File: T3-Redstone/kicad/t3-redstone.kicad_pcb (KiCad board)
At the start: 4 copper layers, 65 x 56.5 mm, 5 parts, among them J1 GEMSTONE_40PIN

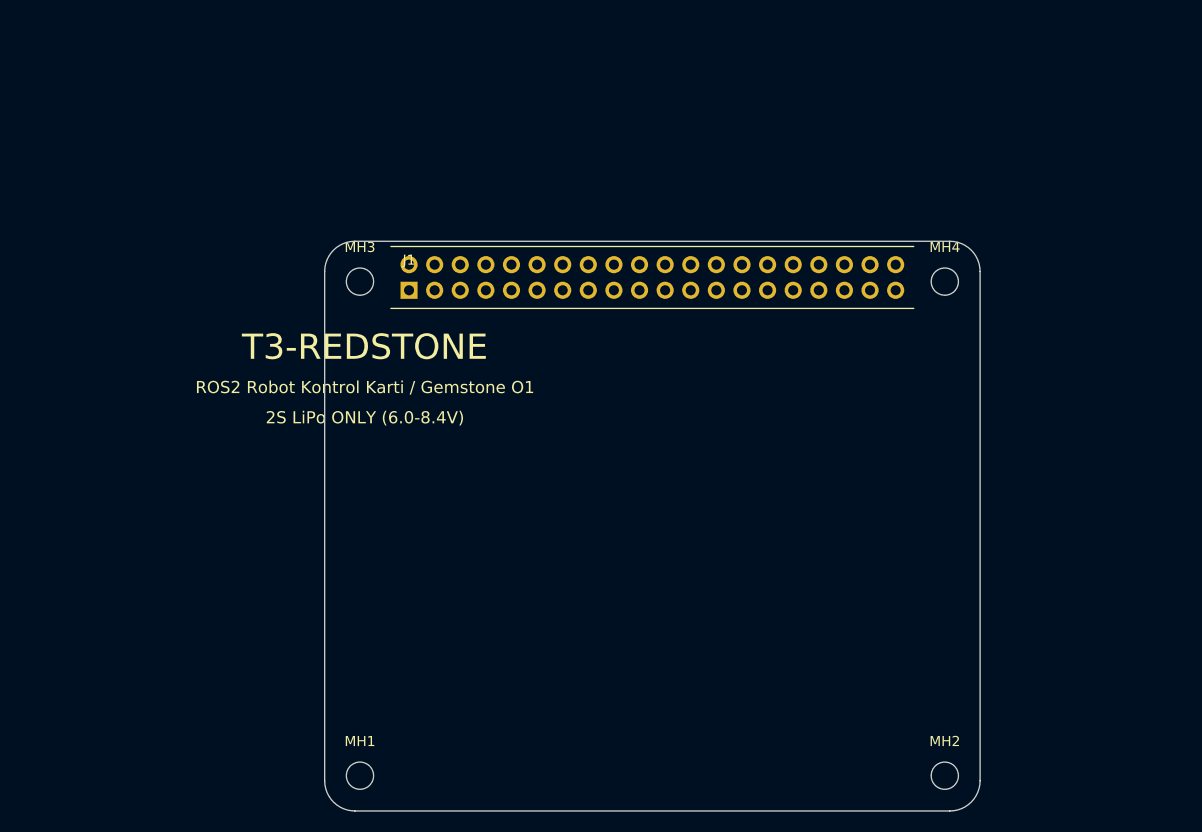
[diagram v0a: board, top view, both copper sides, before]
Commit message: Redstone: tam boy 85x56, kamera/DSI kesiti, 2x20 disi soket
- Kart 65x56.5 (RPi HAT) yerine Gemstone ile ayni tam boy 85x56 mm
- Alt kenara acik U kesit: J4 (CSI) ve J12 (CSI/DSI) konnektorlerine
  kablo ve parmak erisimi. Konum parametrik (CUT_X1/CUT_X2/CUT_DEPTH),
  fotograftan tahmin - kumpasla dogrulanacak
- 2x20 erkek header yerine disi soket (PinSocket_2x20)
- Tam boy shield USB-A yigini ve RJ45 uzerinden gectigi icin en az 16mm
  gecis yuksekliginde soket ve standoff sart; Dwgs.User katmaninda
  yuksek konnektor bolgeleri isaretlendi
- Edge.Cuts konturu kapali dogrulandi (14 segment, 85.00x56.00)

Co-Authored-By: Claude Opus 5 <noreply@anthropic.com>
Claude-Session: https://claude.ai/code/session_01BKimLRXBxXq2q9hJZXs5Qz
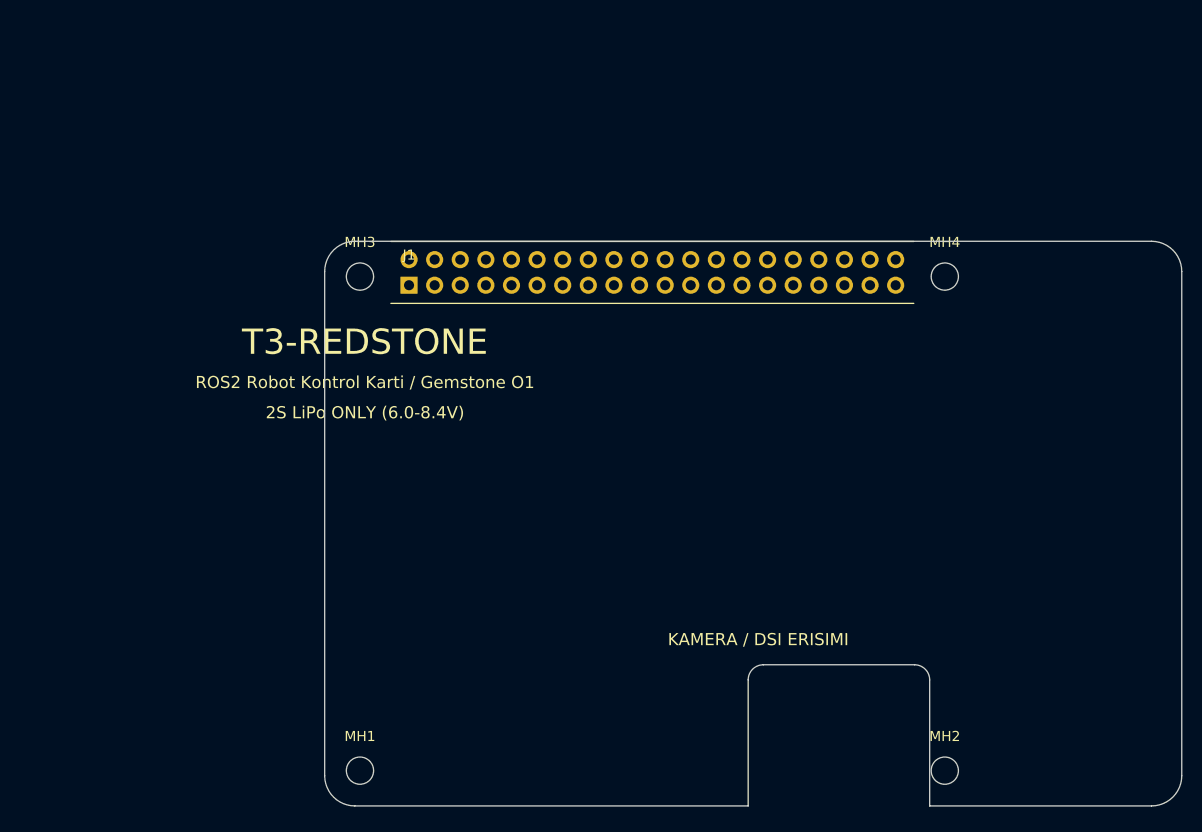
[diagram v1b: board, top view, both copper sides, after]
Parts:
- J1: value GEMSTONE_40PIN -> GEMSTONE_40PIN_DISI_YUKSEK; footprint Connector_PinHeader_2.54mm:PinHeader_2x20_P2.54mm_Vertical -> Connector_PinSocket_2.54mm:PinSocket_2x20_P2.54mm_Vertical
- moved J1 0.50 mm to (58.4, 54.4)
- moved MH1 0.50 mm to (53.5, 102.5)
- moved MH2 0.50 mm to (111.5, 102.5)
- moved MH3 0.50 mm to (53.5, 53.5)
- moved MH4 0.50 mm to (111.5, 53.5)
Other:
- board size 65 x 56.5 mm -> 85 x 56 mm
- board text added: "KAMERA / DSI ERISIMI"
- board text added: "RJ45 Gigabit - h~13.5mm - YUKSEK HEADER SART"
- board text added: "SHIELD = GEMSTONE O1 TAM BOY 85x56"
- board text added: "USB-A x3 yigini - h~13.5mm - YUKSEK HEADER SART"
- board text removed: "GEMSTONE O1 KONTURU 85x56 (referans)"
- board text removed: "USB-A + RJ45 BOLGESI - shield buraya UZANMAMALI (h~13.5mm)"
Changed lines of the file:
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@@
       (subtractmaskfromsilk no) (outputformat 1) (mirror no) (drillshape 1) (scaleselection 1) (outputdirectory "")))
   (net 0 "")
-  (gr_line (start 53.0000 106.5000) (end 112.0000 106.5000) (stroke (width 0.1) (type solid)) (layer "Edge.Cuts"))
-  (gr_line (start 115.0000 103.5000) (end 115.0000 53.0000) (stroke (width 0.1) (type solid)) (layer "Edge.Cuts"))
-  (gr_line (start 112.0000 50.0000) (end 53.0000 50.0000) (stroke (width 0.1) (type solid)) (layer "Edge.Cuts"))
-  (gr_line (start 50.0000 53.0000) (end 50.0000 103.5000) (stroke (width 0.1) (type solid)) (layer "Edge.Cuts"))
-  (gr_arc (start 112.0000 106.5000) (mid 114.1213 105.6213) (end 115.0000 103.5000) (stroke (width 0.1) (type solid)) (layer "Edge.Cuts"))
-  (gr_arc (start 115.0000 53.0000) (mid 114.1213 50.8787) (end 112.0000 50.0000) (stroke (width 0.1) (type solid)) (layer "Edge.Cuts"))
+  (gr_line (start 135.0000 103.0000) (end 135.0000 53.0000) (stroke (width 0.1) (type solid)) (layer "Edge.Cuts"))
+  (gr_line (start 132.0000 50.0000) (end 53.0000 50.0000) (stroke (width 0.1) (type solid)) (layer "Edge.Cuts"))
+  (gr_line (start 50.0000 53.0000) (end 50.0000 103.0000) (stroke (width 0.1) (type solid)) (layer "Edge.Cuts"))
+  (gr_arc (start 132.0000 106.0000) (mid 134.1213 105.1213) (end 135.0000 103.0000) (stroke (width 0.1) (type solid)) (layer "Edge.Cuts"))
+  (gr_arc (start 135.0000 53.0000) (mid 134.1213 50.8787) (end 132.0000 50.0000) (stroke (width 0.1) (type solid)) (layer "Edge.Cuts"))
   (gr_arc (start 53.0000 50.0000) (mid 50.8787 50.8787) (end 50.0000 53.0000) (stroke (width 0.1) (type solid)) (layer "Edge.Cuts"))
-  (gr_arc (start 50.0000 103.5000) (mid 50.8787 105.6213) (end 53.0000 106.5000) (stroke (width 0.1) (type solid)) (layer "Edge.Cuts"))
-  (gr_line (start 50.0000 106.5000) (end 135.0000 106.5000) (stroke (width 0.15) (type solid)) (layer "Dwgs.User"))
-  (gr_line (start 135.0000 106.5000) (end 135.0000 50.5000) (stroke (width 0.15) (type solid)) (layer "Dwgs.User"))
-  (gr_line (start 135.0000 50.5000) (end 50.0000 50.5000) (stroke (width 0.15) (type solid)) (layer "Dwgs.User"))
-  (gr_line (start 50.0000 50.5000) (end 50.0000 106.5000) (stroke (width 0.15) (type solid)) (layer "Dwgs.User"))
-  (gr_text "GEMSTONE O1 KONTURU 85x56 (referans)" (at 84.0000 110.0000) (layer "Dwgs.User") (effects (font (size 1.2 1.2) (thickness 0.25))))
-  (gr_line (start 115.0000 106.5000) (end 135.0000 106.5000) (stroke (width 0.3) (type solid)) (layer "Dwgs.User"))
-  (gr_line (start 135.0000 106.5000) (end 135.0000 50.5000) (stroke (width 0.3) (type solid)) (layer "Dwgs.User"))
-  (gr_line (start 135.0000 50.5000) (end 115.0000 50.5000) (stroke (width 0.3) (type solid)) (layer "Dwgs.User"))
-  (gr_line (start 115.0000 50.5000) (end 115.0000 106.5000) (stroke (width 0.3) (type solid)) (layer "Dwgs.User"))
-  (gr_text "USB-A + RJ45 BOLGESI - shield buraya UZANMAMALI (h~13.5mm)" (at 125.0000 78.5000) (layer "Dwgs.User") (effects (font (size 1.0 1.0) (thickness 0.25))))
-  (footprint "MountingHole:MountingHole_2.7mm_M2.5" (layer "F.Cu") (at 53.5000 103.0000)
+  (gr_arc (start 50.0000 103.0000) (mid 50.8787 105.1213) (end 53.0000 106.0000) (stroke (width 0.1) (type solid)) (layer "Edge.Cuts"))
+  (gr_line (start 53.0000 106.0000) (end 92.0000 106.0000) (stroke (width 0.1) (type solid)) (layer "Edge.Cuts"))
+  (gr_line (start 110.0000 106.0000) (end 132.0000 106.0000) (stroke (width 0.1) (type solid)) (layer "Edge.Cuts"))
+  (gr_line (start 92.0000 106.0000) (end 92.0000 93.5000) (stroke (width 0.1) (type solid)) (layer "Edge.Cuts"))
+  (gr_line (start 110.0000 93.5000) (end 110.0000 106.0000) (stroke (width 0.1) (type solid)) (layer "Edge.Cuts"))
+  (gr_line (start 93.5000 92.0000) (end 108.5000 92.0000) (stroke (width 0.1) (type solid)) (layer "Edge.Cuts"))
+  (gr_arc (start 92.0000 93.5000) (mid 92.4393 92.4393) (end 93.5000 92.0000) (stroke (width 0.1) (type solid)) (layer "Edge.Cuts"))
+  (gr_arc (start 108.5000 92.0000) (mid 109.5607 92.4393) (end 110.0000 93.5000) (stroke (width 0.1) (type solid)) (layer "Edge.Cuts"))
+  (gr_text "SHIELD = GEMSTONE O1 TAM BOY 85x56" (at 80.0000 109.0000) (layer "Dwgs.User") (effects (font (size 1.2 1.2) (thickness 0.25))))
+  (gr_line (start 118.0000 86.0000) (end 135.0000 86.0000) (stroke (width 0.3) (type solid)) (layer "Dwgs.User"))
+  (gr_line (start 135.0000 86.0000) (end 135.0000 54.0000) (stroke (width 0.3) (type solid)) (layer "Dwgs.User"))
+  (gr_line (start 135.0000 54.0000) (end 118.0000 54.0000) (stroke (width 0.3) (type solid)) (layer "Dwgs.User"))
+  (gr_line (start 118.0000 54.0000) (end 118.0000 86.0000) (stroke (width 0.3) (type solid)) (layer "Dwgs.User"))
+  (gr_text "USB-A x3 yigini - h~13.5mm - YUKSEK HEADER SART" (at 126.5000 70.0000) (layer "Dwgs.User") (effects (font (size 1.0 1.0) (thickness 0.25))))
+  (gr_line (start 110.0000 106.0000) (end 135.0000 106.0000) (stroke (width 0.3) (type solid)) (layer "Dwgs.User"))
+  (gr_line (start 135.0000 106.0000) (end 135.0000 88.0000) (stroke (width 0.3) (type solid)) (layer "Dwgs.User"))
+  (gr_line (start 135.0000 88.0000) (end 110.0000 88.0000) (stroke (width 0.3) (type solid)) (layer "Dwgs.User"))
+  (gr_line (start 110.0000 88.0000) (end 110.0000 106.0000) (stroke (width 0.3) (type solid)) (layer "Dwgs.User"))
+  (gr_text "RJ45 Gigabit - h~13.5mm - YUKSEK HEADER SART" (at 122.5000 97.0000) (layer "Dwgs.User") (effects (font (size 1.0 1.0) (thickness 0.25))))
+  (footprint "MountingHole:MountingHole_2.7mm_M2.5" (layer "F.Cu") (at 53.5000 102.5000)
     (property "Reference" "MH1" (at 0 -3.4 0) (layer "F.SilkS") (effects (font (size 1 1) (thickness 0.15))))
     (property "Value" "M2.5" (at 0 3.4 0) (layer "F.Fab") (hide yes) (effects (font (size 1 1) (thickness 0.15))))
@@
     (fp_circle (center 0 0) (end 3.2 0) (stroke (width 0.15) (type solid)) (fill none) (layer "F.CrtYd"))
   )
-  (footprint "MountingHole:MountingHole_2.7mm_M2.5" (layer "F.Cu") (at 111.5000 103.0000)
+  (footprint "MountingHole:MountingHole_2.7mm_M2.5" (layer "F.Cu") (at 111.5000 102.5000)
     (property "Reference" "MH2" (at 0 -3.4 0) (layer "F.SilkS") (effects (font (size 1 1) (thickness 0.15))))
     (property "Value" "M2.5" (at 0 3.4 0) (layer "F.Fab") (hide yes) (effects (font (size 1 1) (thickness 0.15))))
@@
     (fp_circle (center 0 0) (end 3.2 0) (stroke (width 0.15) (type solid)) (fill none) (layer "F.CrtYd"))
   )
-  (footprint "MountingHole:MountingHole_2.7mm_M2.5" (layer "F.Cu") (at 53.5000 54.0000)
+  (footprint "MountingHole:MountingHole_2.7mm_M2.5" (layer "F.Cu") (at 53.5000 53.5000)
     (property "Reference" "MH3" (at 0 -3.4 0) (layer "F.SilkS") (effects (font (size 1 1) (thickness 0.15))))
     (property "Value" "M2.5" (at 0 3.4 0) (layer "F.Fab") (hide yes) (effects (font (size 1 1) (thickness 0.15))))
@@
     (fp_circle (center 0 0) (end 3.2 0) (stroke (width 0.15) (type solid)) (fill none) (layer "F.CrtYd"))
   )
-  (footprint "MountingHole:MountingHole_2.7mm_M2.5" (layer "F.Cu") (at 111.5000 54.0000)
+  (footprint "MountingHole:MountingHole_2.7mm_M2.5" (layer "F.Cu") (at 111.5000 53.5000)
     (property "Reference" "MH4" (at 0 -3.4 0) (layer "F.SilkS") (effects (font (size 1 1) (thickness 0.15))))
     (property "Value" "M2.5" (at 0 3.4 0) (layer "F.Fab") (hide yes) (effects (font (size 1 1) (thickness 0.15))))
@@
     (fp_circle (center 0 0) (end 3.2 0) (stroke (width 0.15) (type solid)) (fill none) (layer "F.CrtYd"))
   )
-  (footprint "Connector_PinHeader_2.54mm:PinHeader_2x20_P2.54mm_Vertical" (layer "F.Cu") (at 58.3660 54.8590)
+  (footprint "Connector_PinSocket_2.54mm:PinSocket_2x20_P2.54mm_Vertical" (layer "F.Cu") (at 58.3660 54.3590)
     (property "Reference" "J1" (at 0 -3 0) (layer "F.SilkS") (effects (font (size 1 1) (thickness 0.15))))
-    (property "Value" "GEMSTONE_40PIN" (at 24 5 0) (layer "F.Fab") (effects (font (size 1 1) (thickness 0.15))))
+    (property "Value" "GEMSTONE_40PIN_DISI_YUKSEK" (at 24 5 0) (layer "F.Fab") (effects (font (size 1 1) (thickness 0.15))))
     (pad "1" thru_hole rect (at 0.000 0.000) (size 1.7 1.7) (drill 1.0) (layers "*.Cu" "*.Mask"))
     (pad "2" thru_hole circle (at 0.000 -2.540) (size 1.7 1.7) (drill 1.0) (layers "*.Cu" "*.Mask"))
@@
     (fp_line (start -1.8 -4.34) (end 50.060 -4.34) (stroke (width 0.12) (type solid)) (layer "F.SilkS"))
   )
-  (gr_text "T3-REDSTONE" (at 54.0000 60.5000) (layer "F.SilkS") (effects (font (size 2.5 2.5) (thickness 0.4))))
-  (gr_text "ROS2 Robot Kontrol Karti / Gemstone O1" (at 54.0000 64.5000) (layer "F.SilkS") (effects (font (size 1.2 1.2) (thickness 0.25))))
-  (gr_text "2S LiPo ONLY (6.0-8.4V)" (at 54.0000 67.5000) (layer "F.SilkS") (effects (font (size 1.2 1.2) (thickness 0.25))))
+  (gr_text "T3-REDSTONE" (at 54.0000 60.0000) (layer "F.SilkS") (effects (font (size 2.5 2.5) (thickness 0.4))))
+  (gr_text "ROS2 Robot Kontrol Karti / Gemstone O1" (at 54.0000 64.0000) (layer "F.SilkS") (effects (font (size 1.2 1.2) (thickness 0.25))))
+  (gr_text "2S LiPo ONLY (6.0-8.4V)" (at 54.0000 67.0000) (layer "F.SilkS") (effects (font (size 1.2 1.2) (thickness 0.25))))
+  (gr_text "KAMERA / DSI ERISIMI" (at 93.0000 89.5000) (layer "F.SilkS") (effects (font (size 1.2 1.2) (thickness 0.25))))
 )
